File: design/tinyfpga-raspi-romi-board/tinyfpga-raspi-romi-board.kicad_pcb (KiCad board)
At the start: 2 copper layers, 103.4 x 121.3 mm, 72 parts, among them J1 TINYFPGA_J1, J10 ROMI_ENC_LEFT, J11 ROMI_ENC_RIGHT, J12 QTR_LEFT, J13 QTR_RIGHT, J14 SONAR_LEFT, J15 SONAR_RIGHT, J16 PWR_SEL1, J17 PWR_SEL0, J18 RPI_EXTRA, J19 ON_OFF, J2 TINYFPGA_J2, J20 ROMI_POWER, J3 Raspberry_Pi_2_3, J4 TINYFPGA_J4, J5 TINYFPGA_J5, J6 WP_JUMP, J7 ROMI_VSW, J8 FUSE_JUMP, J9 ROMI_MOTOR_DRIVE, Q1 2N7000, Q2 2N7000, Q3 2N7000, Q4 2N7000, Q5 2N7000, Q6 2N7000, Q7 2N7000, Q8 2N7000, SW2 SW_Push, SW3 SW_Push, SW4 SW_Push, U1 CAT24C128

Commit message: happy with power section
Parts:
- moved R24 42.0 mm to (37.3, 49.5), turned to 0 degrees
- moved R10 37.2 mm to (37.3, 44.5), turned to 0 degrees
- moved U1 20.6 mm to (138.9, 131.1)
- moved J6 19.9 mm to (139.8, 125.3)
- moved R22 18.6 mm to (145.5, 128.3)
- moved R2 18.4 mm to (145.5, 131.1)
- moved R1 18.1 mm to (145.5, 133.9)
- moved J16 15.5 mm to (113.9, 122.2), turned to 270 degrees
- moved J17 12.0 mm to (113.9, 127.0), turned to 270 degrees
- moved D1 8.54 mm to (96.5, 139.8), turned to 90 degrees
- moved C2 8.35 mm to (84.3, 138.8)
- moved C1 5.34 mm to (89.7, 138.9), turned to 90 degrees
- moved R9 5.11 mm to (132.7, 45.0), turned to 0 degrees
- moved A1 4.87 mm to (74.0, 134.0)
- moved F1 4.85 mm to (78.0, 140.6)
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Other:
- board text added: "3.3V"
- board text added: "5V OFF"
- board text added: "CUT THE ROMI VREG_SET TRACE BEFORE CONNECTING THIS BOARD TO BASE!!"
- board text added: "FPGA"
- board text added: "ONBOARD"
- board text added: "ONBOARD SOURCE"
- board text added: "ROMI"
- board text added: "RPI"
- board text removed: "CUT THE ROMI VREG_SET TRACE BEFORE CONNECTING BOARD!!"
- board text removed: "SHORT FOR 5V OFF"

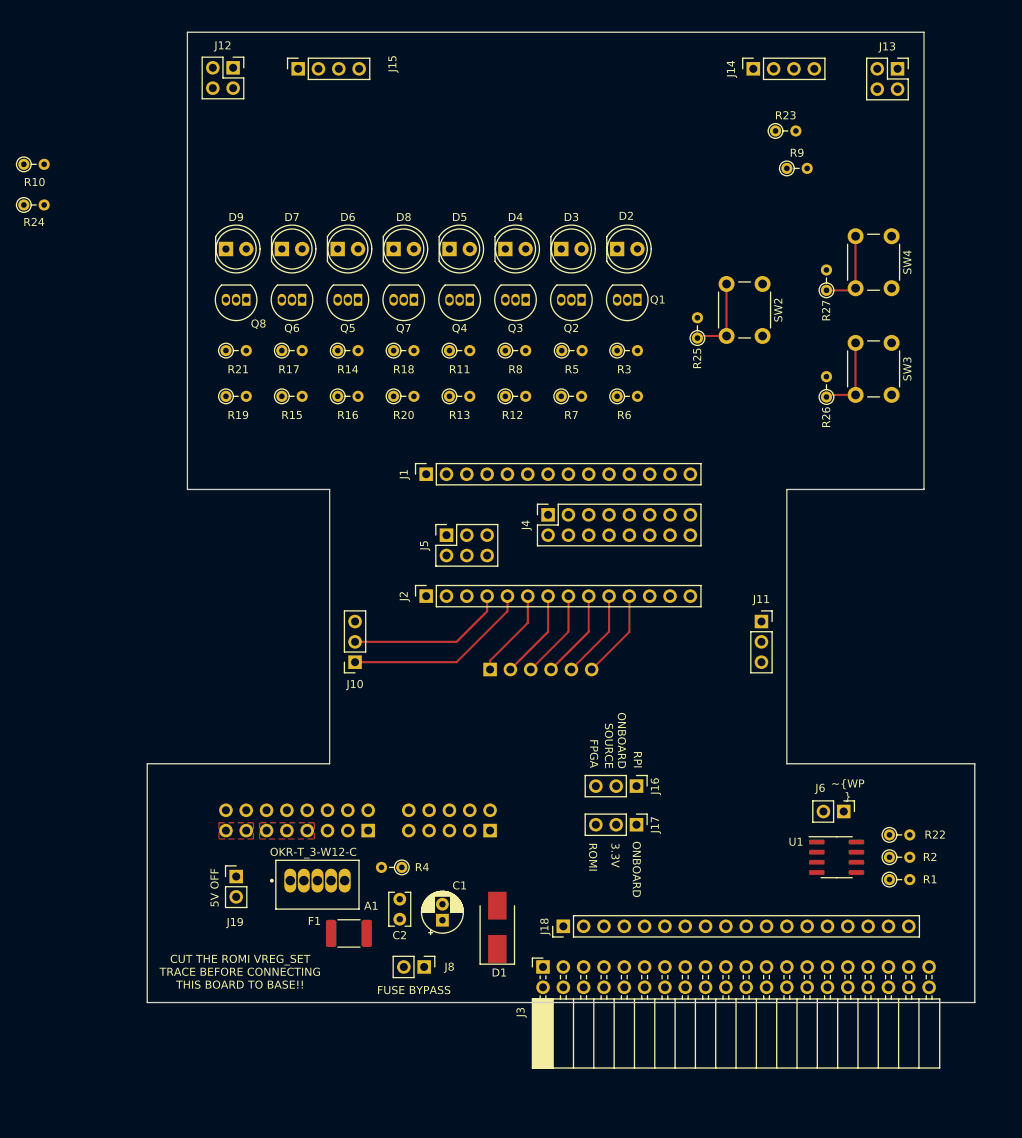
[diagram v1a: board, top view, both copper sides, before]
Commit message: happy with mechanicals. routing and pin swapping
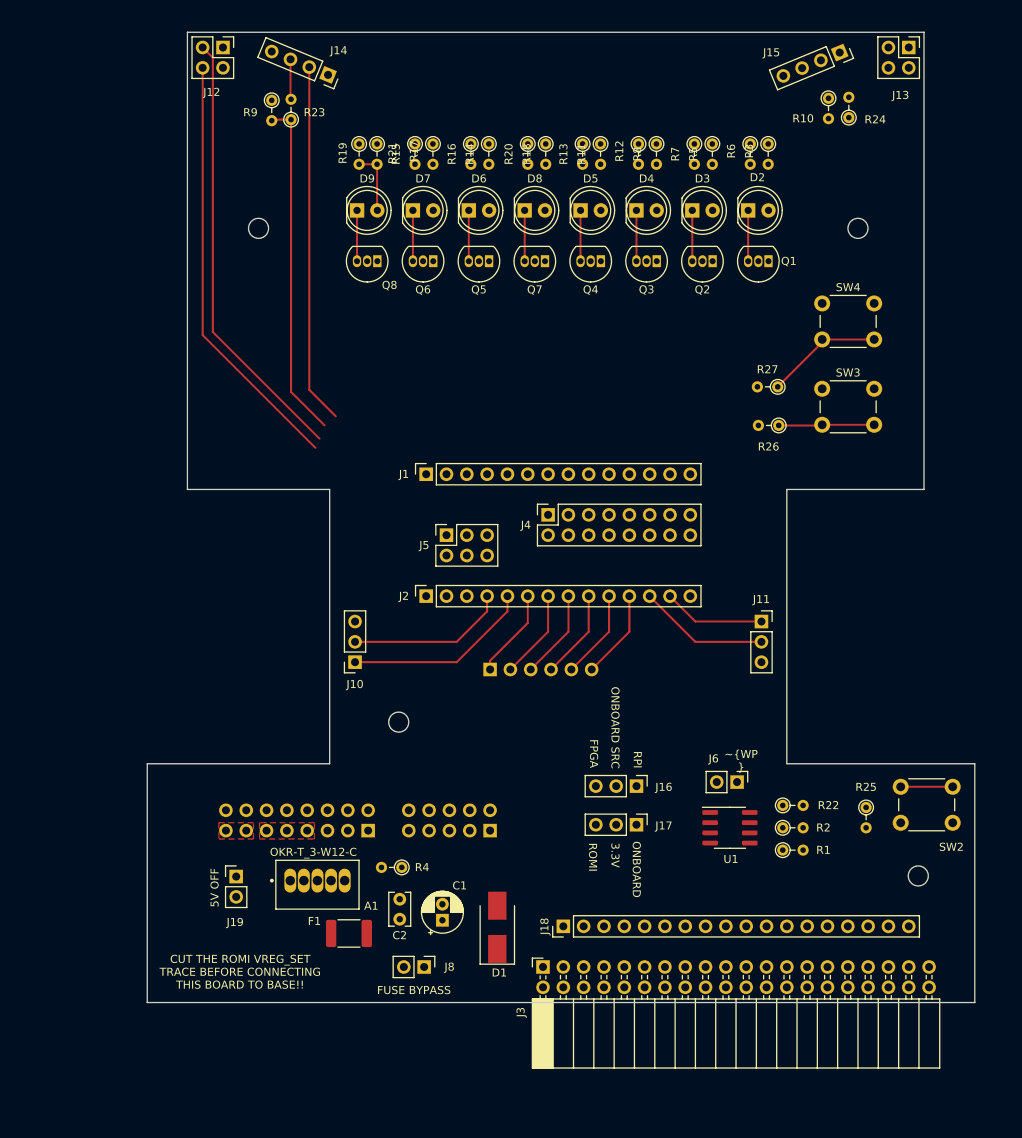
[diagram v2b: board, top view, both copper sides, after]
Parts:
- added H1: MountingHole, MountingHole:MountingHole_2.5mm, F.Cu at (149.1, 133.4)
- added H2: MountingHole, MountingHole:MountingHole_2.5mm, F.Cu at (84.2, 114.2)
- added H3: MountingHole, MountingHole:MountingHole_2.5mm, F.Cu at (66.7, 52.5)
- added H4: MountingHole, MountingHole:MountingHole_2.5mm, F.Cu at (141.6, 52.5)
- moved R24 103.7 mm to (140.5, 38.6), turned to 90 degrees
- moved R10 100.9 mm to (137.9, 36.2), turned to 270 degrees
- moved SW2 71.4 mm to (153.4, 126.8), turned to 180 degrees
- moved J15 67.7 mm to (139.3, 30.5), turned to 292.5 degrees
- moved R9 64.9 mm to (68.3, 36.4), turned to 270 degrees
- moved R25 62.3 mm to (142.6, 124.8), turned to 270 degrees
- moved R23 60.6 mm to (70.7, 38.9), turned to 90 degrees
- moved J14 53.2 mm to (75.4, 33.3), turned to 247.5 degrees
- moved R20 35.7 mm to (100.3, 41.9), turned to 270 degrees
- moved R12 35.7 mm to (114.2, 41.9), turned to 270 degrees
- moved R13 35.7 mm to (107.2, 41.9), turned to 270 degrees
- moved R15 35.7 mm to (86.2, 41.9), turned to 270 degrees
- moved R16 35.7 mm to (93.2, 41.9), turned to 270 degrees
- moved R19 35.7 mm to (79.2, 41.9), turned to 270 degrees
- moved R6 35.7 mm to (128.1, 41.9), turned to 270 degrees
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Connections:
- J1 pad 4: /FPGA_BTN_RST -> /FPGA_HBA_INT
- J18 pad 4: /RPI_GPIO4 -> (no net)
- J18 pad 5: /RPI_GPIO13 -> (no net)
- J3 pad 33: /RPI_GPIO13 -> /FPGA_HBA_INT
- J3 pad 7: /RPI_GPIO4 -> /RPI_BTN0
- R25 pad 1: /FPGA_BTN_RST -> /RPI_BTN0
- SW2 pad 2: /FPGA_BTN_RST -> /RPI_BTN0
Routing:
- net /QTRL_OUT: track 0.00 -> 54.9 mm
- net /QTRL_CTRL: track 0.00 -> 53.3 mm
- net /SONL_TRIG: track 0.00 -> 45.0 mm
- net /SONL_ECHO: track 0.00 -> 42.4 mm
- net /ROMI_ENC_RB: track 0.00 -> 16.3 mm
- net /ROMI_ENC_RA: track 0.00 -> 12.7 mm
- net /FPGA_BTN_RST: track 10.2 -> 0.00 mm
- net Net-(D9-Pad2): track 0.00 -> 8.02 mm
- net /RPI_BTN0: track 0.00 -> 6.50 mm
- net Net-(D9-Pad1): track 0.00 -> 6.35 mm
- net Net-(D8-Pad1): track 0.00 -> 6.35 mm
- net Net-(D7-Pad1): track 0.00 -> 6.35 mm
- net Net-(D6-Pad1): track 0.00 -> 6.35 mm
- net Net-(D5-Pad1): track 0.00 -> 6.35 mm
- net Net-(D4-Pad1): track 0.00 -> 6.35 mm
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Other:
- board text added: "ONBOARD SRC"
- board text removed: "ONBOARD SOURCE"

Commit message: mostly done routing but have a few more rpi signals to deal with
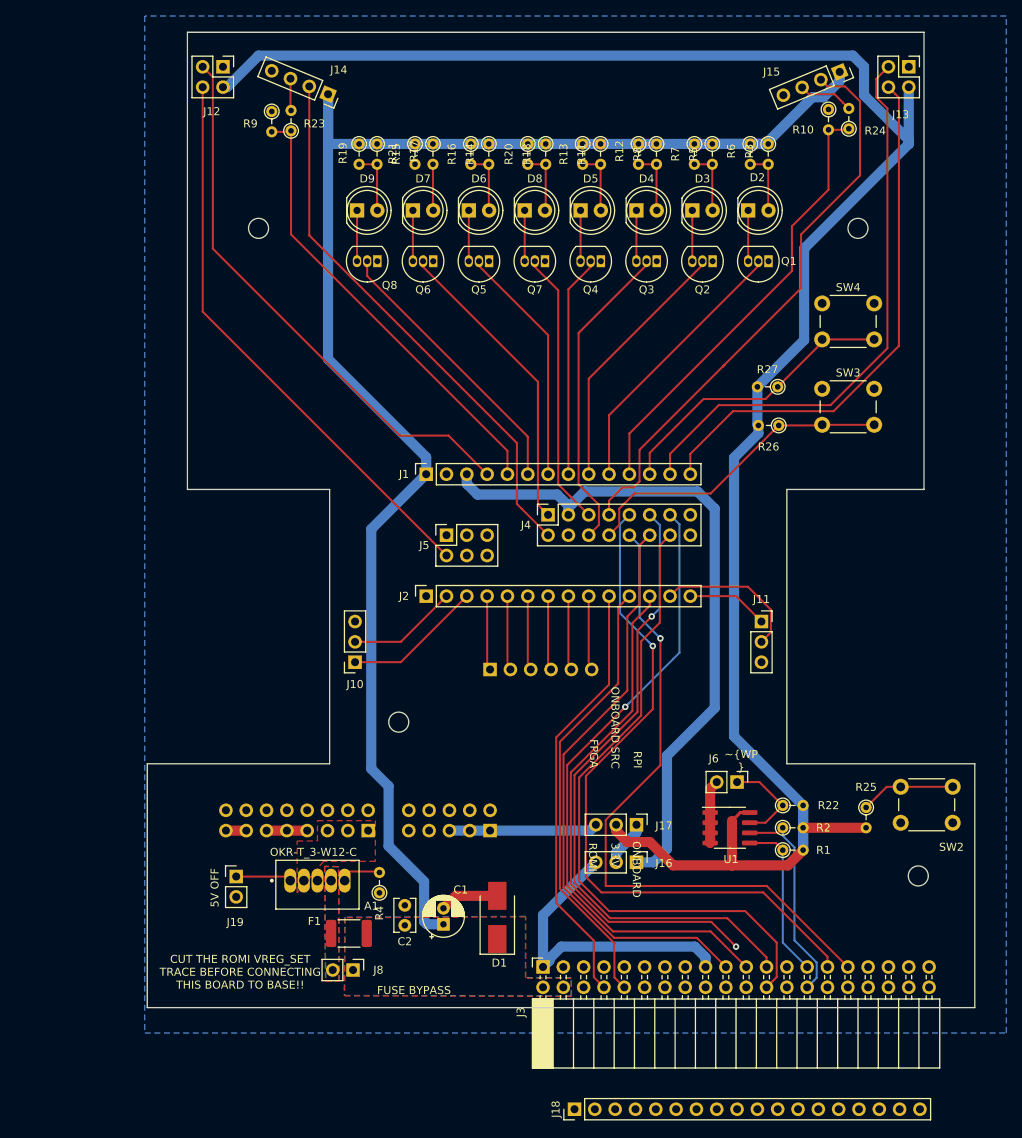
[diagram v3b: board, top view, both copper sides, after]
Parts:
- moved J18 22.9 mm to (106.2, 162.6)
- moved J16 9.53 mm to (113.9, 131.7)
- moved J8 8.90 mm to (78.5, 145.2)
- moved R4 4.23 mm to (81.8, 135.5), turned to 90 degrees
- moved J12 2.41 mm to (62.2, 32.3)
- moved J13 2.41 mm to (148.0, 32.3)
- moved J14 2.41 mm to (75.4, 35.7)
- moved J15 2.41 mm to (139.3, 32.9)
- moved R24 1.40 mm to (140.5, 40.0)
- moved R10 1.40 mm to (137.9, 37.6)
- moved R23 1.40 mm to (70.7, 40.3)
- moved R9 1.40 mm to (68.3, 37.8)
- moved D1 1.24 mm to (96.5, 138.6)
- moved C2 0.99 mm to (85.0, 139.6)
- moved C1 0.52 mm to (89.8, 139.4)
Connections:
- net Net-(A1-Pad4) renamed /VREG_OUT
- net Net-(J7-Pad11) renamed /VRP
- net Net-(J7-Pad13) renamed /VB
- J1 pad 10: /SONR_ECHO -> /FPGA_LED0
- J1 pad 11: /QTRR_CTRL -> /SONR_ECHO
- J1 pad 12: /QTRR_OUT -> /FPGA_BTN1
- J1 pad 13: /QTRL_CTRL -> /QTRR_OUT
- J1 pad 14: /QTRL_OUT -> /QTRR_CTRL
- J1 pad 4: /FPGA_HBA_INT -> /QTRL_OUT
- J1 pad 5: /RPI_TXD -> /SONL_ECHO
- J1 pad 6: /RPI_RXD -> /FPGA_LED7
- J1 pad 7: /SONL_TRIG -> /FPGA_LED2
- J1 pad 8: /SONL_ECHO -> /FPGA_LED5
- J1 pad 9: /SONR_TRIG -> /FPGA_LED4
- J2 pad 10: /ROMI_DIRR -> /RPI_TXD
- J2 pad 11: /ROMI_PWMR -> /RPI_RXD
- J2 pad 12: /ROMI_ENC_RB -> /FPGA_HBA_INT
- J2 pad 13: /ROMI_ENC_RA -> /ROMI_ENC_RB
- J2 pad 14: /FPGA_LED0 -> /ROMI_ENC_RA
- J2 pad 2: /FPGA_BTN0 -> /ROMI_ENC_LB
- J2 pad 3: /FPGA_BTN1 -> /ROMI_ENC_LA
- J2 pad 4: /ROMI_ENC_LB -> /ROMI_~SLPL
- J2 pad 5: /ROMI_ENC_LA -> /ROMI_DIRL
- J2 pad 6: /ROMI_~SLPL -> /ROMI_PWML
- J2 pad 7: /ROMI_DIRL -> /ROMI_~SLPR
- J2 pad 8: /ROMI_PWML -> /ROMI_DIRR
- J2 pad 9: /ROMI_~SLPR -> /ROMI_PWMR
- J4 pad 1: /FPGA_LED1 -> /FPGA_LED6
- J4 pad 2: /FPGA_LED4 -> /SONL_TRIG
- J4 pad 5: /FPGA_LED2 -> /FPGA_LED3
- J4 pad 6: /FPGA_LED5 -> /FPGA_LED1
- J4 pad 7: /FPGA_LED3 -> /SONR_TRIG
- J4 pad 8: /FPGA_LED6 -> /FPGA_BTN0
- J5 pad 2: /FPGA_LED7 -> /QTRL_CTRL
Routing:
- net +3V3: track 0.00 -> 250.8 mm
- net +5V: track 0.00 -> 198.2 mm
- net /FPGA_3.3V_OUT: track 0.00 -> 86.6 mm
- net /FPGA_~HOLD: track 0.00 -> 86.5 mm, vias 0 -> 1
- net /FPGA_~WP: track 0.00 -> 82.8 mm, vias 0 -> 1
- net /FPGA_SS: track 0.00 -> 81.9 mm
- net /FPGA_SCK: track 0.00 -> 80.0 mm, vias 0 -> 1
- net /FPGA_SDO: track 0.00 -> 79.2 mm, vias 0 -> 1
- net /FPGA_SDI: track 0.00 -> 72.9 mm
- net /SONR_TRIG: track 0.00 -> 71.8 mm
- net /QTRR_OUT: track 0.00 -> 71.6 mm
- net /QTRR_CTRL: track 0.00 -> 67.1 mm
- net /FPGA_HBA_INT: track 0.00 -> 64.0 mm, vias 0 -> 1
- net /SONR_ECHO: track 0.00 -> 56.0 mm
- net /RPI_RXD: track 0.00 -> 55.8 mm
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- added copper zone on B.Cu, net +5V
- added copper zone on F.Cu, net +5V
- added copper zone on F.Cu, net +BATT
- added copper zone on B.Cu, net /VREG_OUT
- added copper zone on F.Cu, net /VREG_OUT
- added copper zone on B.Cu, net GND
- removed copper zone on F.Cu, net /VB
- removed copper zone on F.Cu, net /VRP
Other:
- board size 103.4 x 121.3 mm -> 103.4 x 121.9 mm
- net class Power added: clearance 0.254, trace_width 1.27, via_dia 0.8, via_drill 0.4

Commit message: signals routed. needs silk and drc
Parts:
- removed J18: RPI_EXTRA, Connector_PinHeader_2.54mm:PinHeader_1x18_P2.54mm_Vertical
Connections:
- J3 pad 11: /RPI_GPIO17 -> (no net)
- J3 pad 12: /RPI_GPIO18 -> (no net)
- J3 pad 13: /ROMI_SHDN -> (no net)
- J3 pad 15: /RPI_GPIO22 -> (no net)
- J3 pad 16: /RPI_GPIO23 -> (no net)
- J3 pad 18: /RPI_GPIO24 -> (no net)
- J3 pad 22: /RPI_GPIO25 -> /FPGA_HBA_INT
- J3 pad 26: /RPI_GPIO7 -> (no net)
- J3 pad 3: /RPI_GPIO2 -> /ROMI_SHDN
- J3 pad 32: /RPI_GPIO12 -> (no net)
- J3 pad 33: /FPGA_HBA_INT -> /RPI_BTN0
- J3 pad 35: /RPI_GPIO19 -> (no net)
- J3 pad 36: /RPI_GPIO16 -> (no net)
- J3 pad 37: /ROMI_PG -> (no net)
- J3 pad 38: /RPI_GPIO20 -> (no net)
- J3 pad 40: /RPI_GPIO21 -> (no net)
- J3 pad 5: /RPI_GPIO3 -> /ROMI_PG
- J3 pad 7: /RPI_BTN0 -> (no net)
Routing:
- net /ROMI_SHDN: track 0.00 -> 29.6 mm
- net /ROMI_PG: track 0.00 -> 28.4 mm
- net /RPI_BTN0: track 11.9 -> 33.9 mm
- net /FPGA_HBA_INT: track 64.0 -> 71.1 mm, vias 1 -> 0
- net Net-(D7-Pad2): track 5.78 -> 8.02 mm
- net +3V3: track 250.8 -> 249.2 mm
- net /FPGA_~WP: track 82.8 -> 81.6 mm
- net /FPGA_SS: track 81.9 -> 81.0 mm
- added copper zone on F.Cu, net GND

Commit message: rev-a sent to fab
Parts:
- removed the J1 at (87.6, 83.2)
- added J2: TINYFPGA_J1, Connector_PinSocket_2.54mm:PinSocket_1x14_P2.54mm_Vertical, F.Cu at (87.6, 83.2)
- moved J13 3.59 mm to (145.4, 34.8), turned to 180 degrees
- moved J12 3.59 mm to (59.7, 34.8), turned to 180 degrees
- renumbered J2 to J1
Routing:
- net /QTRL_OUT: track 69.2 -> 65.6 mm
- net /QTRL_CTRL: track 71.2 -> 73.6 mm
- net +3V3: track 249.2 -> 247.5 mm
- net /QTRR_OUT: track 71.6 -> 69.9 mm
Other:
- board text added: "3.3V POWER SELECT"
- board text added: "5V POWER"
- board text added: "CUT ROMI VREG_SET BEFORE CONNECTING THIS BOARD TO BASE!!"
- board text added: "DEVICE TREE EEPROM"
- board text added: "FPGA USER BUTTON 0"
- board text added: "FPGA USER BUTTON 1"
- board text added: "Homebrew Automation Romi Adapter Board Rev. A (190626)"
- board text added: "ONBOARD POWER SELECT"
- board text added: "RASPBERRY PI"
- board text added: "REFLECT_LEFT"
- board text added: "REFLECT_RIGHT"
- board text added: "RPI USER BUTTON"
- board text added: "SONAR_LEFT"
- board text added: "SONAR_RIGHT"
- board text removed: "3.3V"
- board text removed: "CUT THE ROMI VREG_SET TRACE BEFORE CONNECTING THIS BOARD TO BASE!!"
- board text removed: "ONBOARD SRC"

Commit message: cleaned up bom
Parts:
- H1, H2, H3, H4: footprint MountingHole:MountingHole_2.5mm -> MountingHole:MountingHole_2.7mm_M2.5
- J1: value TINYFPGA_J2 -> Conn_01x14_Female
- J10: value ROMI_ENC_LEFT -> PinSocket_1x03_P2.54mm_Vertical
- J11: value ROMI_ENC_RIGHT -> PinSocket_1x03_P2.54mm_Vertical
- J12: value QTR_LEFT -> PinSocket_2x02_P2.54mm_Vertical
- J13: value QTR_RIGHT -> PinSocket_2x02_P2.54mm_Vertical
- J14: value SONAR_LEFT -> PinSocket_1x04_P2.54mm_Vertical
- J15: value SONAR_RIGHT -> PinSocket_1x04_P2.54mm_Vertical
- J16: value PWR_SEL1 -> PinHeader_1x03_P2.54mm_Vertical
- J17: value PWR_SEL0 -> PinHeader_1x03_P2.54mm_Vertical
- J2: value TINYFPGA_J1 -> Conn_01x14_Female
- J20: value ROMI_POWER -> PinHeader_2x05_P2.54mm_Vertical
- J4: value TINYFPGA_J4 -> PinSocket_2x08_P2.54mm_Vertical
- J5: value TINYFPGA_J5 -> PinSocket_2x03_P2.54mm_Vertical
- J6: value WP_JUMP -> PinHeader_1x02_P2.54mm_Vertical
- J7: value ROMI_VSW -> PinHeader_2x08_P2.54mm_Vertical
- J8: value FUSE_JUMP -> PinHeader_1x02_P2.54mm_Vertical
- J9: value ROMI_MOTOR_DRIVE -> PinHeader_1x06_P2.54mm_Vertical
